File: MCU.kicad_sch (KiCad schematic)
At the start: 37 parts, among them CN10 Conn_02x02_Odd_Even, CN6 Conn_02x02_Odd_Even, CN7 Conn_02x08_Odd_Even, CN8 Conn_02x04_Odd_Even, CN9 Conn_02x05_Odd_Even, IC110 CXK5816, IC112 M41464, IC113 M41464, IC130 D91061GD, IC132 74HC245, IC133 74HC245

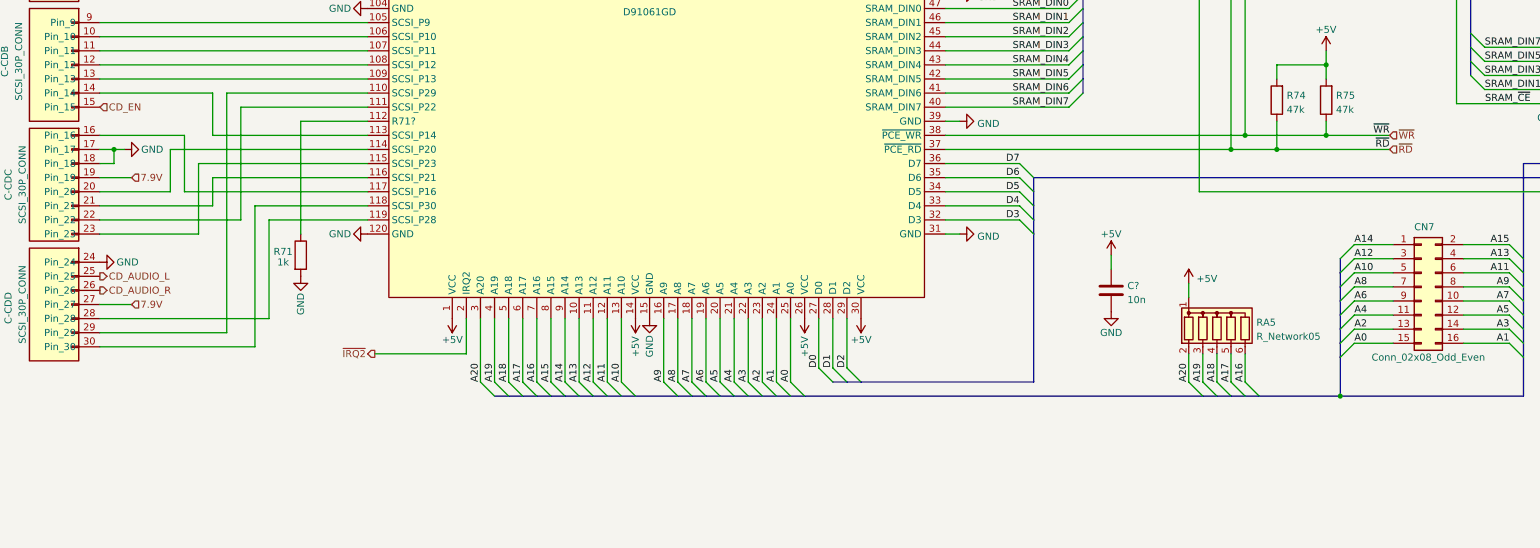
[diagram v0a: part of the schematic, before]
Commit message: PCE expansion port added with only relevant pins.
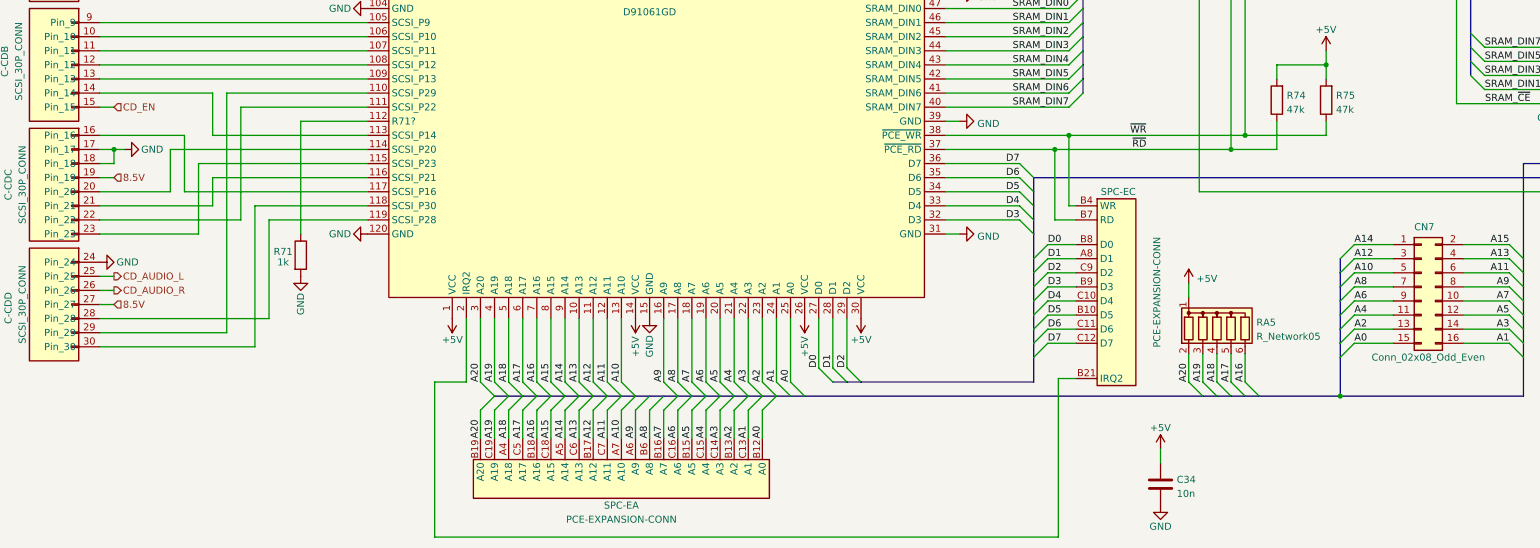
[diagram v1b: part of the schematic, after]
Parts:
- added SPC-E: PCE-EXPANSION-CONN, symbol IFU-30:PCE-EXPANSION-CONN
- gave numbers to parts that had none: 1
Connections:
- net A0: now also SPC-E.B12 (A0)
- net A1: now also SPC-E.C13 (A1)
- net A10: now also SPC-E.A7 (A10)
- net A11: now also SPC-E.C7 (A11)
- net A12: now also SPC-E.B17 (A12)
- net A13: now also SPC-E.C6 (A13)
- net A14: now also SPC-E.A5 (A14)
- net A15: now also SPC-E.C18 (A15)
- net A16: now also SPC-E.B18 (A16)
- net A17: now also SPC-E.C5 (A17)
- net A18: now also SPC-E.A4 (A18)
- net A19: now also SPC-E.C19 (A19)
- net A2: now also SPC-E.B13 (A2)
- net A20: now also SPC-E.B19 (A20)
- net A3: now also SPC-E.C14 (A3)
- net A4: now also SPC-E.C15 (A4)
- net A5: now also SPC-E.B15 (A5)
- net A6: now also SPC-E.C16 (A6)
- net A7: now also SPC-E.B16 (A7)
- net A8: now also SPC-E.B6 (A8)
- net A9: now also SPC-E.A6 (A9)
- net D0: now also SPC-E.B8 (D0)
- net D1: now also SPC-E.A8 (D1)
- net D2: now also SPC-E.C9 (D2)
- net D3: now also SPC-E.B9 (D3)
- net D4: now also SPC-E.C10 (D4)
- net D5: now also SPC-E.B10 (D5)
- net D6: now also SPC-E.C11 (D6)
- net D7: now also SPC-E.C12 (D7)
- net ~{RD}: now also SPC-E.B7 (RD)
- net ~{WR}: now also SPC-E.B4 (WR)
- net 7.9V renamed 8.5V
- net ~{IRQ2}: no longer names the net of IC130.2 (IRQ2)
- net ~{IRQ2}: now also SPC-E.B21 (IRQ2)
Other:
- moved on the sheet: C34

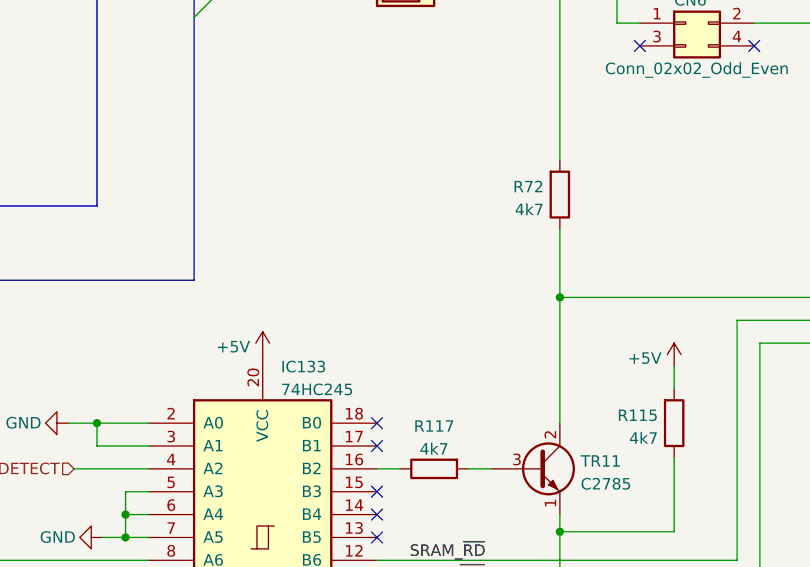
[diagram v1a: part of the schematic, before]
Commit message: Fixed mistake in ADPCM page and added notes about opamps.
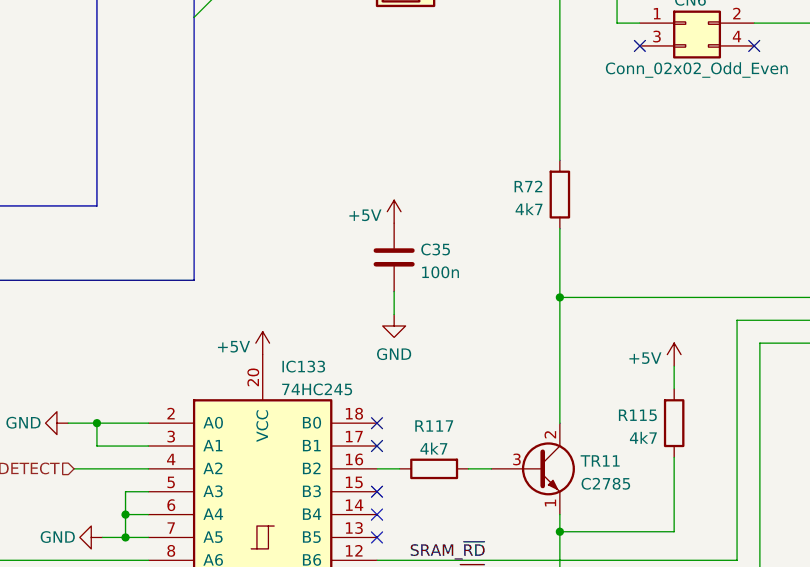
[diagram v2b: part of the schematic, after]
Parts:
- added C35: 100n, symbol Device:C
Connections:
- net +5V: now also C35.2
- net GND: now also C35.1
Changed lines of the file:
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@@
+    (stroke (width 0) (type default) (color 0 0 0 0))
+  )
+  (wire (pts (xy 290.195 125.095) (xy 290.195 127.635))
     (stroke (width 0) (type default) (color 0 0 0 0))
   )
@@
     )
     (property "Datasheet" "" (id 3) (at 245.11 38.1 0)
+      (effects (font (size 1.27 1.27)) hide)
+    )
+    (pin "1")
+  )
+  (symbol (lib_id "power:GND") (at 290.195 127.635 0) (unit 1)
+    (in_bom yes) (on_board yes) (fields_autoplaced)
+    (property "Reference" "#PWR?" (id 0) (at 290.195 133.985 0)
+      (effects (font (size 1.27 1.27)) hide)
+    )
+    (property "Value" "GND" (id 1) (at 290.195 132.0784 0))
+    (property "Footprint" "" (id 2) (at 290.195 127.635 0)
+      (effects (font (size 1.27 1.27)) hide)
+    )
+    (property "Datasheet" "" (id 3) (at 290.195 127.635 0)
       (effects (font (size 1.27 1.27)) hide)
     )
@@
     )
     (property "Datasheet" "" (id 3) (at 219.71 71.12 0)
+      (effects (font (size 1.27 1.27)) hide)
+    )
+    (pin "1")
+  )
+  (symbol (lib_id "power:+5V") (at 290.195 117.475 0) (mirror y) (unit 1)
+    (in_bom yes) (on_board yes)
+    (property "Reference" "#PWR?" (id 0) (at 290.195 121.285 0)
+      (effects (font (size 1.27 1.27)) hide)
+    )
+    (property "Value" "+5V" (id 1) (at 288.798 116.6388 0)
+      (effects (font (size 1.27 1.27)) (justify left))
+    )
+    (property "Footprint" "" (id 2) (at 290.195 117.475 0)
+      (effects (font (size 1.27 1.27)) hide)
+    )
+    (property "Datasheet" "" (id 3) (at 290.195 117.475 0)
       (effects (font (size 1.27 1.27)) hide)
     )
@@
       (effects (font (size 1.27 1.27)) hide)
     )
+    (pin "1")
+    (pin "2")
+  )
+  (symbol (lib_id "Device:C") (at 290.195 121.285 180) (unit 1)
+    (in_bom yes) (on_board yes) (fields_autoplaced)
+    (property "Reference" "C35" (id 0) (at 293.116 120.4503 0)
+      (effects (font (size 1.27 1.27)) (justify right))
+    )
+    (property "Value" "100n" (id 1) (at 293.116 122.9872 0)
+      (effects (font (size 1.27 1.27)) (justify right))
+    )
+    (property "Footprint" "" (id 2) (at 289.2298 117.475 0)
+      (effects (font (size 1.27 1.27)) hide)
+    )
+    (property "Datasheet" "~" (id 3) (at 290.195 121.285 0)
+      (effects (font (size 1.27 1.27)) hide)
+    )

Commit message: Documentation started.
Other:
- title: (none) -> NEC PC-Engine IFU-30
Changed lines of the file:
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@@
   (paper "A3")
   (title_block
-    (date "2022-10-23")
+    (title "NEC PC-Engine IFU-30")
+    (date "2022-10-27")
+    (rev "0.1")
+    (comment 1 "Author: Regis Galland")
+    (comment 2 "NEC IFU-30 PCB reverse engineered schematics")
   )
   (junction (at 137.16 85.725) (diameter 0) (color 0 0 0 0)

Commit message: Documentation update
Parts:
- renumbered C-CD to C-CD1, SPC-E to SPC-E1
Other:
- moved on the sheet: SPC-E1A

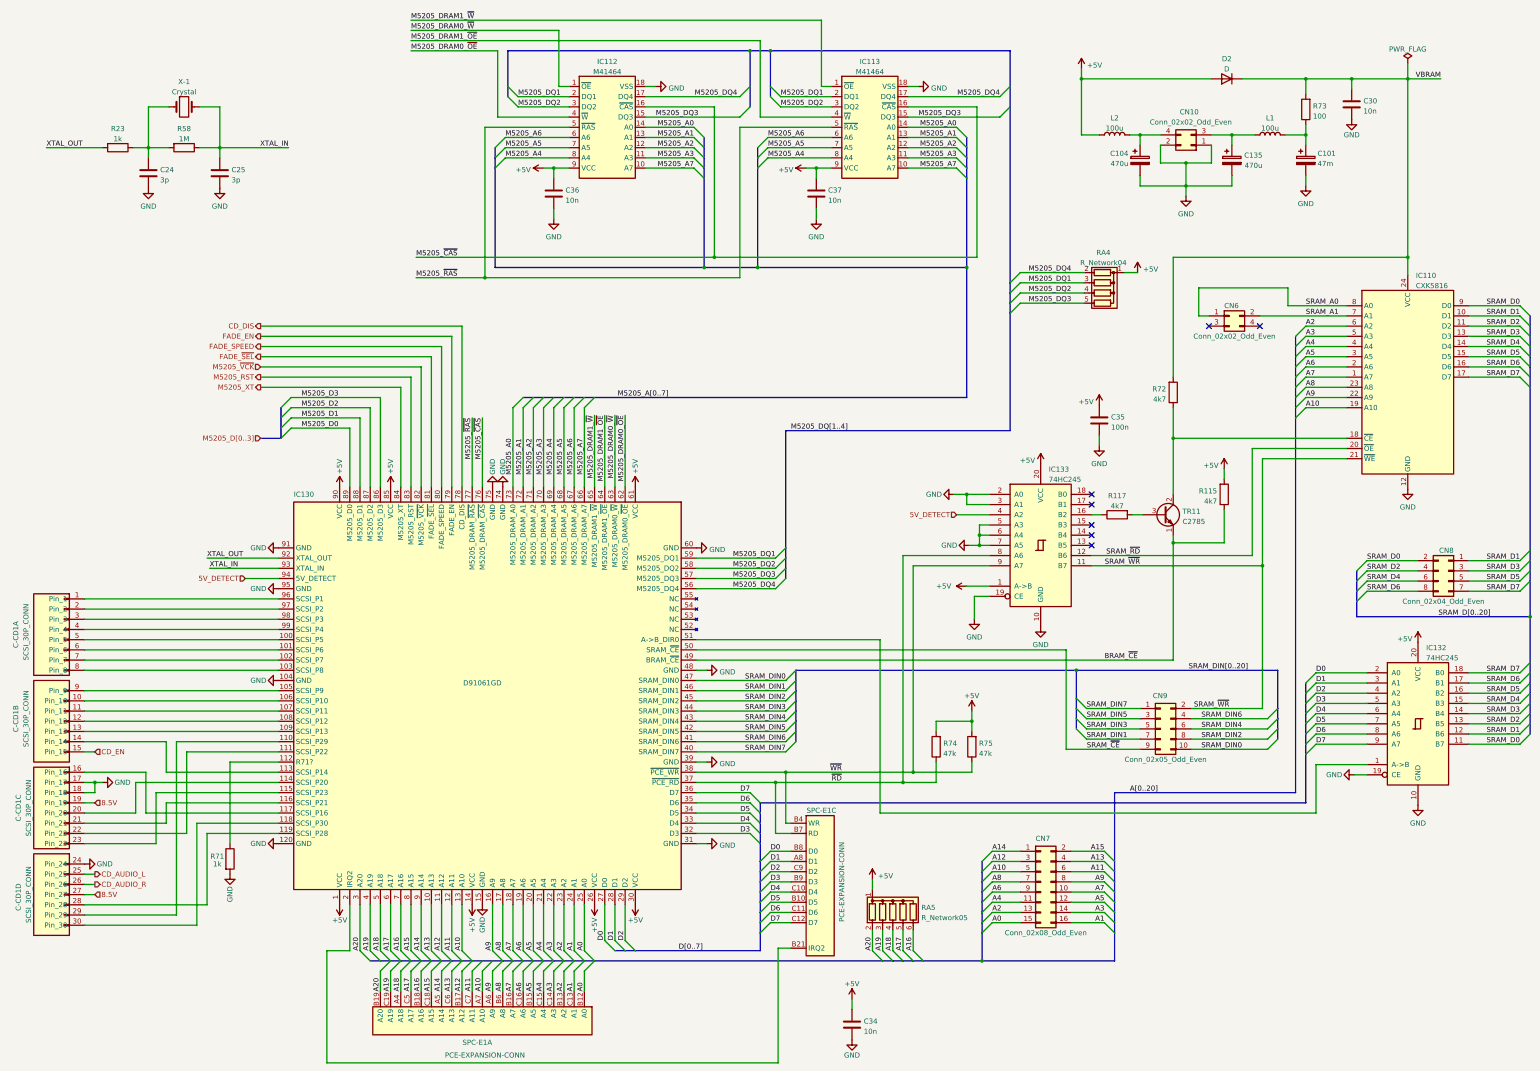
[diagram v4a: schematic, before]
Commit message: Unsused pins from expansion conenctor on 1 page. CD conenctor signals added.
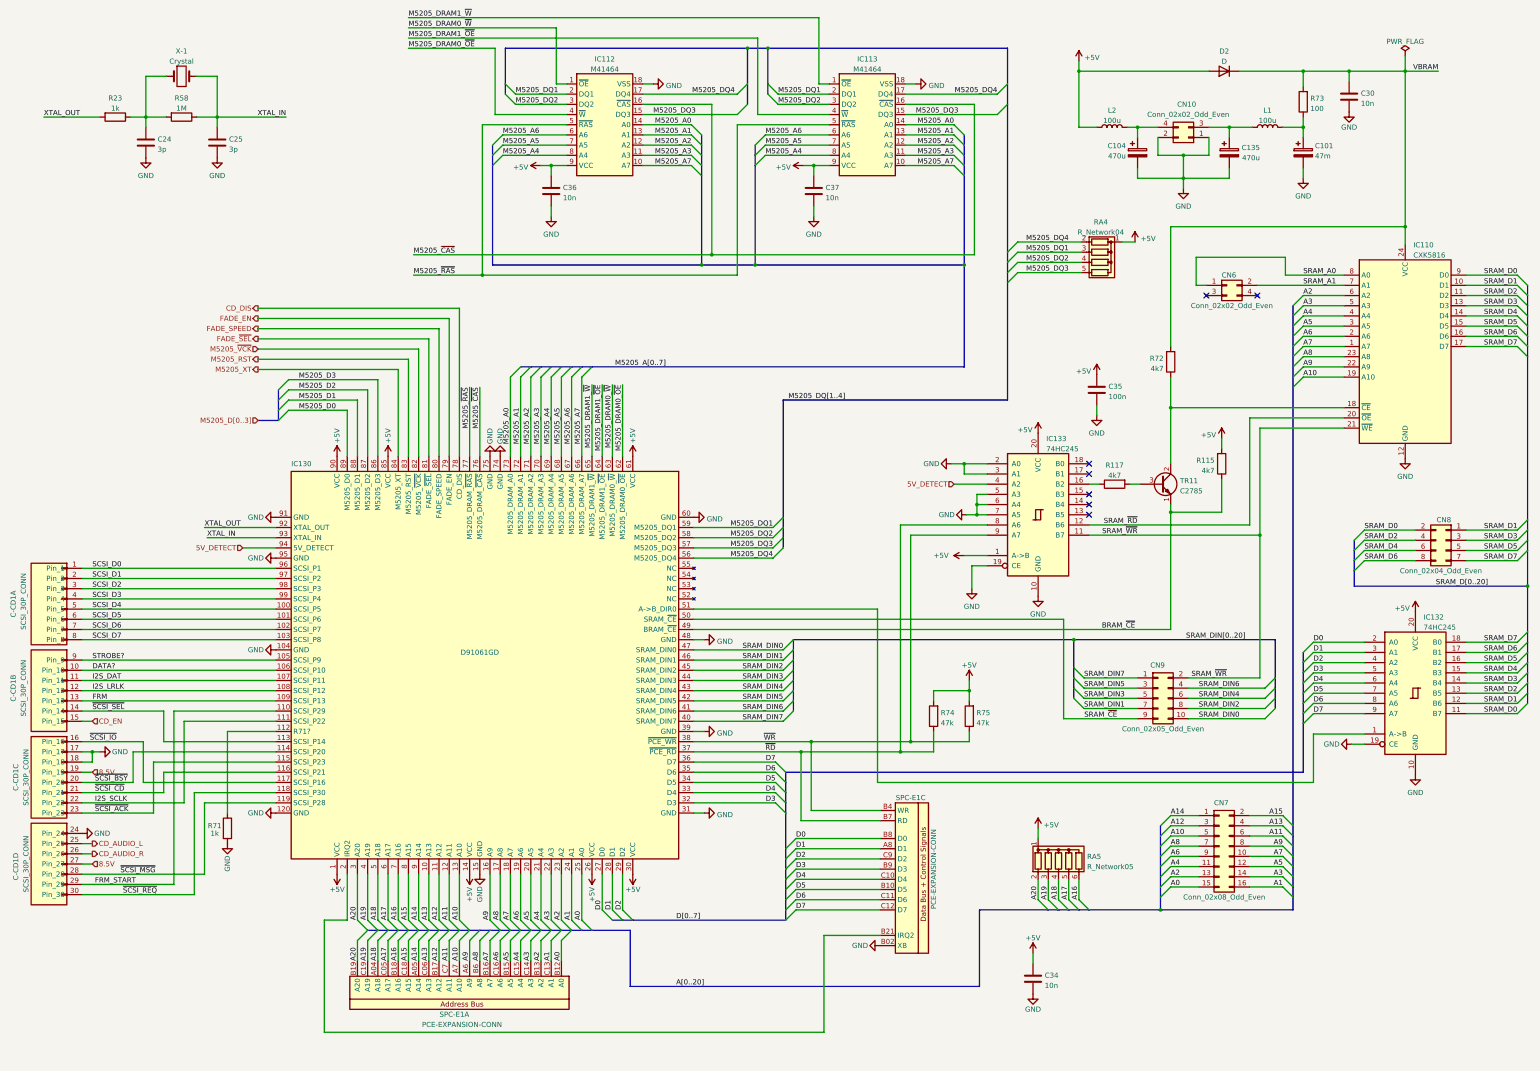
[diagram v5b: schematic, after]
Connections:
- net A13: now also SPC-E1.C06 (A13); no longer SPC-E1.C6 (A13)
- net A14: now also SPC-E1.A05 (A14); no longer SPC-E1.A5 (A14)
- net A17: now also SPC-E1.C05 (A17); no longer SPC-E1.C5 (A17)
- net A18: now also SPC-E1.A04 (A18); no longer SPC-E1.A4 (A18)
- net GND: now also SPC-E1.B02 (XB)
- net SCSI_D4: now reaches C-CD1.5 (Pin_5), IC130.100 (SCSI_P5)
- net SCSI_D5: now reaches C-CD1.6 (Pin_6), IC130.101 (SCSI_P6)
- net SCSI_D6: now reaches C-CD1.7 (Pin_7), IC130.102 (SCSI_P7)
- net SCSI_D7: now reaches C-CD1.8 (Pin_8), IC130.103 (SCSI_P8)
- net STROBE?: now reaches C-CD1.9 (Pin_9), IC130.105 (SCSI_P9)
- net DATA?: now reaches C-CD1.10 (Pin_10), IC130.106 (SCSI_P10)
- net I2S_DAT: now reaches C-CD1.11 (Pin_11), IC130.107 (SCSI_P11)
- net I2S_LRLK: now reaches C-CD1.12 (Pin_12), IC130.108 (SCSI_P12)
- net FRM: now reaches C-CD1.13 (Pin_13), IC130.109 (SCSI_P13)
- net FRM_START: now reaches C-CD1.29 (Pin_29), IC130.110 (SCSI_P29)
- net I2S_SCLK: now reaches C-CD1.22 (Pin_22), IC130.111 (SCSI_P22)
- net ~{SCSI_SEL}: now reaches C-CD1.14 (Pin_14), IC130.113 (SCSI_P14)
- net ~{SCSI_BSY}: now reaches C-CD1.20 (Pin_20), IC130.114 (SCSI_P20)
- net ~{SCSI_ACK}: now reaches C-CD1.23 (Pin_23), IC130.115 (SCSI_P23)
- net ~{SCSI_CD}: now reaches C-CD1.21 (Pin_21), IC130.116 (SCSI_P21)
- net ~{SCSI_IO}: now reaches C-CD1.16 (Pin_16), IC130.117 (SCSI_P16)
- net ~{SCSI_REQ}: now reaches C-CD1.30 (Pin_30), IC130.118 (SCSI_P30)
- net ~{SCSI_MSG}: now reaches C-CD1.28 (Pin_28), IC130.119 (SCSI_P28)
- net SCSI_D0: now reaches C-CD1.1 (Pin_1), IC130.96 (SCSI_P1)
- net SCSI_D1: now reaches C-CD1.2 (Pin_2), IC130.97 (SCSI_P2)
- net SCSI_D2: now reaches C-CD1.3 (Pin_3), IC130.98 (SCSI_P3)
- net SCSI_D3: now reaches C-CD1.4 (Pin_4), IC130.99 (SCSI_P4)
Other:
- moved on the sheet: C-CD1A, C-CD1B, C-CD1C, C-CD1D, C101, C104, C135, C24, C25, C30, C34, C35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

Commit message: Fixed a few typos and mainly renamed connections to CD-ROM with more accurate descriptions
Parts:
- C-CD1: value SCSI_30P_CONN -> 30P_ELCO_5061; symbol IFU-30:SCSI_30P_CONN -> IFU-30:30P_ELCO_5061; Manufacturer (none) -> KYOCERA AVX; Manufacturer Part Number (none) -> 105061030103856+; Supplier (none) -> Digikey; Supplier Part Number (none) -> 478-105061030103856+-ND
- SPC-E1: footprint (none) -> IFU-30:PinSocket_3x23_P2.54mm_Horizontal
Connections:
- net 8.5V: now also C-CD1.B8 (+9V), C-CD1.B9 (+9V); no longer C-CD1.19 (Pin_19), C-CD1.27 (Pin_27)
- net A10: now also SPC-E1.A07 (A10); no longer SPC-E1.A7 (A10)
- net A11: now also SPC-E1.C07 (A11); no longer SPC-E1.C7 (A11)
- net A8: now also SPC-E1.B06 (A8); no longer SPC-E1.B6 (A8)
- net A9: now also SPC-E1.A06 (A9); no longer SPC-E1.A6 (A9)
- net CD_AUDIO_L: now also C-CD1.B12 (AUDIO_L); no longer C-CD1.25 (Pin_25)
- net CD_AUDIO_R: now also C-CD1.B10 (AUDIO_R); no longer C-CD1.26 (Pin_26)
- net D0: now also SPC-E1.B08 (D0); no longer SPC-E1.B8 (D0)
- net D1: now also SPC-E1.A08 (D1); no longer SPC-E1.A8 (D1)
- net D2: now also SPC-E1.C09 (D2); no longer SPC-E1.C9 (D2)
- net D3: now also SPC-E1.B09 (D3); no longer SPC-E1.B9 (D3)
- net GND: now also C-CD1.B11 (GNDA), C-CD1.B13 (GND), C-CD1.B14 (GND); no longer C-CD1.17 (Pin_17), C-CD1.18 (Pin_18), C-CD1.24 (Pin_24)
- net I2S_DAT: now also C-CD1.A10 (I2S_DAT); no longer C-CD1.11 (Pin_11)
- net I2S_SCLK: now also C-CD1.B3 (I2S_SCLK); no longer C-CD1.22 (Pin_22)
- net SCSI_D0: now also C-CD1.A15 (SCSI_D0); no longer C-CD1.1 (Pin_1)
- net SCSI_D1: now also C-CD1.A13 (SCSI_D1); no longer C-CD1.2 (Pin_2)
- net SCSI_D2: now also C-CD1.A11 (SCSI_D2); no longer C-CD1.3 (Pin_3)
- net SCSI_D3: now also C-CD1.A9 (SCSI_D3); no longer C-CD1.4 (Pin_4)
- net SCSI_D4: now also C-CD1.A7 (SCSI_D4); no longer C-CD1.5 (Pin_5)
- net SCSI_D5: now also C-CD1.A5 (SCSI_D5); no longer C-CD1.6 (Pin_6)
- net SCSI_D6: now also C-CD1.A3 (SCSI_D6); no longer C-CD1.7 (Pin_7)
- net SCSI_D7: now also C-CD1.A1 (SCSI_D7); no longer C-CD1.8 (Pin_8)
- net ~{RD}: now also SPC-E1.B07 (RD); no longer SPC-E1.B7 (RD)
- net ~{SCSI_ACK}: now also C-CD1.B1 (~{SCSI_ACK}); no longer C-CD1.23 (Pin_23)
- net ~{SCSI_BSY}: now also C-CD1.B7 (~{SCSI_BSY}); no longer C-CD1.20 (Pin_20)
- net ~{SCSI_CD}: now also C-CD1.B5 (~{SCSI_CD}); no longer C-CD1.21 (Pin_21)
- net ~{SCSI_IO}: now also C-CD1.B15 (~{SCSI_IO}); no longer C-CD1.16 (Pin_16)
- net ~{SCSI_MSG}: now also C-CD1.B6 (~{SCSI_MSG}); no longer C-CD1.28 (Pin_28)
- net ~{SCSI_REQ}: now also C-CD1.B2 (~{SCSI_REQ}); no longer C-CD1.30 (Pin_30)
- net ~{SCSI_SEL}: now also C-CD1.A4 (~{SCSI_SEL}); no longer C-CD1.14 (Pin_14)
- net ~{WR}: now also SPC-E1.B04 (WR); no longer SPC-E1.B4 (WR)
- removed net CD_EN: C-CD1.15 (Pin_15)
- net DATA? renamed PW
- net PW: now also C-CD1.A12 (PW); no longer C-CD1.10 (Pin_10)
- net FRM renamed SFSY
- net SFSY: now also C-CD1.A6 (SFSY); no longer C-CD1.13 (Pin_13)
- net FRM_START renamed SBSY
- net SBSY: now also C-CD1.B4 (SBSY); no longer C-CD1.29 (Pin_29)
- net I2S_LRLK renamed I2S_LRCK
- net I2S_LRCK: now also C-CD1.A8 (I2S_LRCK); no longer C-CD1.12 (Pin_12)
- net STROBE? renamed SBCK
- net SBCK: now also C-CD1.A14 (SBCK); no longer C-CD1.9 (Pin_9)
- new net ~{CD_RST}: C-CD1.A2 (~{SCSI_RST})
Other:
- moved on the sheet: C101, C24, C25, C30, C34, C35, C36, C37, CN6, CN8, IC110, IC112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
